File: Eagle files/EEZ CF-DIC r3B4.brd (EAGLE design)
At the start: 155 x 85 mm, 244 parts, among them IC1 MC79L05, IC2 LP2951, IC3 VIPer35L, IC4 SI8233BB-D-IS1, IC5 LM5041B, IC6 IR11688STRPBF, IC7 TL072, IC8 TL103W, IC9 TL431, P1 T910W-50K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

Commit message: Optional temperature alarm
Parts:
- added C75: 100n, rcl:C0603
- added IC10: LM211PWR, EEZ_Lib1:PW8_TSSOP8
- added NTC1: 10K, EEZ_Lib1:R_0805
- added R81: 100K, rcl:R0805
- added R82, R84: 10K, rcl:R0805
- added R83: N.C., rcl:R0805
- R15: value N.C. -> 10K
- R16: value 10K -> N.C.
- R80: value N.C. -> 1K
- moved EEZ_SIGNATURE 138.4 mm to (156.0, 76.6), turned to 270 degrees
- moved R15 58.6 mm to (13.7, 57.0), flipped to the bottom, turned to 270 degrees
- moved R16 58.6 mm to (70.3, 72.1), flipped to the top, turned to 90 degrees
- moved R80 7.85 mm to (24.3, 41.1), turned to 90 degrees
- moved R71 1.94 mm to (59.9, 29.3), turned to 0 degrees
- moved C72 1.39 mm to (56.1, 33.0), turned to 90 degrees
- moved R72 1.39 mm to (58.0, 33.0), turned to 90 degrees
- moved R65 1.06 mm to (55.9, 29.3), turned to 0 degrees
- moved C58 0.51 mm to (11.0, 42.6)
- moved R57 0.45 mm to (48.6, 8.76)
- moved Q8 0.45 mm to (42.1, 20.4)
- moved R56 0.44 mm to (44.6, 8.76)
- moved C46 0.38 mm to (87.2, 35.9)
- moved C67 0.38 mm to (47.6, 40.2)
- moved C59 0.32 mm to (10.5, 44.8)
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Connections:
- new net +2.5VREF: C72.1, IC8.3, NTC1.1, P1.E, R66.2, R72.1, R80.2
- new net N$34: IC10.3, NTC1.2, R84.2
- net AUX: now also R16.2; no longer R15.2
- net FB: now also R83.2; no longer R80.2
- net GND: now also C75.2, IC10.1, IC10.4, R82.2, R83.1, R84.1; no longer R80.1
- net N$141: now also R16.1; no longer R15.1
- net N$7: now also IC10.2, R80.1, R81.2, R82.1; no longer C72.1, IC8.3, P1.E, R66.2, R72.1
- net PWRGOOD: now also IC10.7, R15.2, R81.1; no longer R16.2
- net V+: now also C75.1, IC10.8, R15.1; no longer R16.1
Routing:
- net +2.5VREF: track 0.00 -> 86.2 mm, vias 0 -> 6
- net N$7: track 66.4 -> 11.0 mm, vias 5 -> 0
- net N$34: track 0.00 -> 32.0 mm, vias 0 -> 1
- net PWRGOOD: track 32.8 -> 59.0 mm, vias 2 -> 4
- net S2_OUT: track 26.6 -> 23.5 mm
- net FB: track 62.3 -> 59.4 mm
- net POUT+: track 30.1 -> 28.8 mm
- net SR_OUT2: track 5.68 -> 4.64 mm
- net S1_DOT_OUT: track 27.5 -> 28.3 mm
- net GND: track 132.2 -> 132.3 mm, vias 12 -> 13
- net V+: track 149.8 -> 149.9 mm, vias 3 -> 4
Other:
- board text added: "(08/2018 r3B4)"
- board text added: "C75"
- board text added: "IC10"
- board text added: "NTC1"
- board text added: "R81"
- board text added: "R82"
- board text added: "R83"
- board text added: "R84"
- board text removed: "(08/2018 r3B3)"

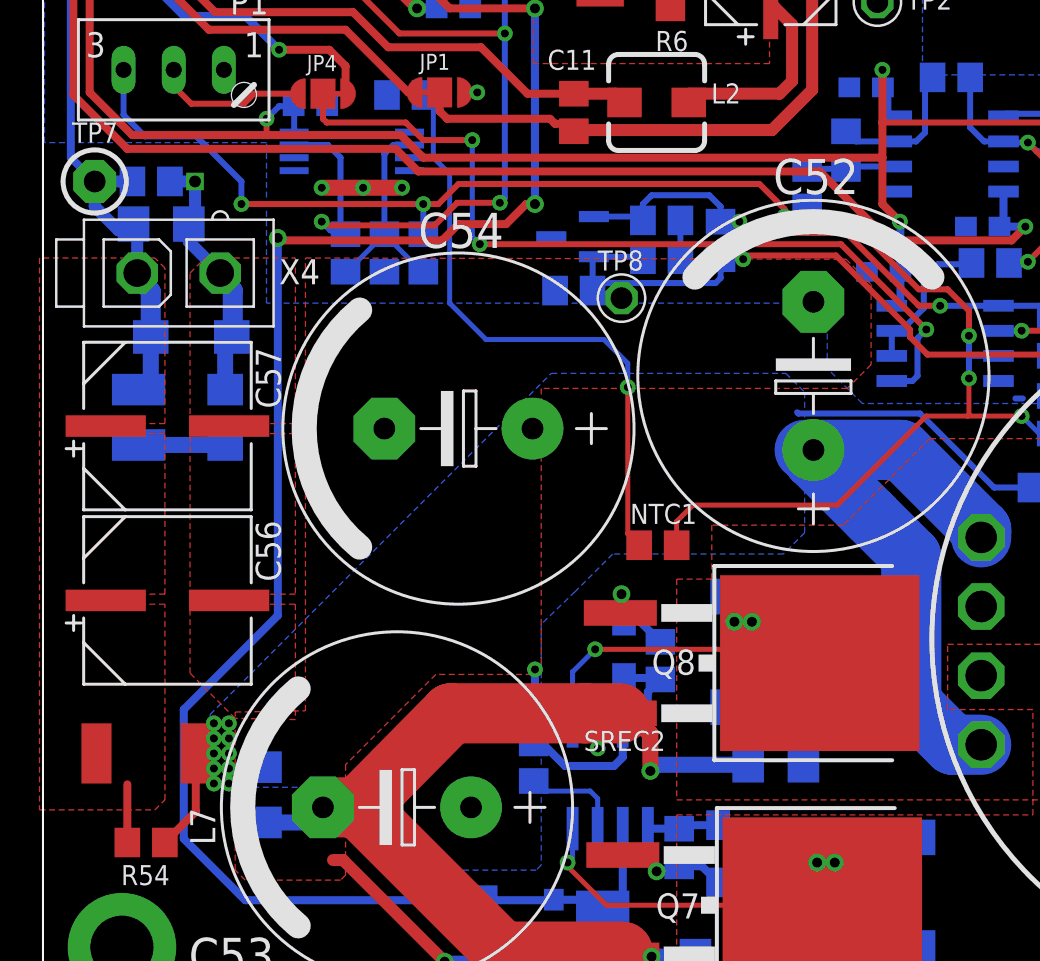
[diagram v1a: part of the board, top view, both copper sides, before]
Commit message: New values for temp. comparator
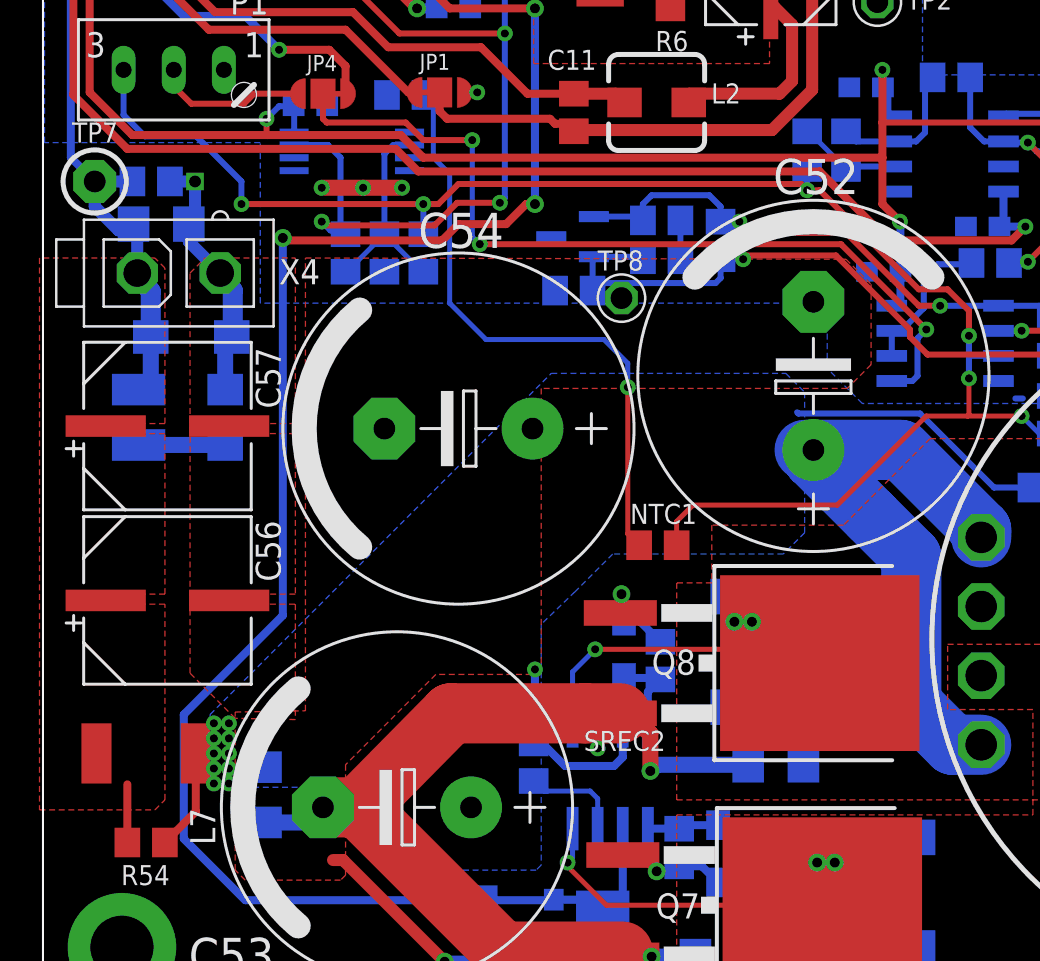
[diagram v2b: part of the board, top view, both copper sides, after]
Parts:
- NTC1: value 10K -> 10K/3570K
- R80: value 1K -> 3K9
- R81: value 100K -> 82K
- R82: value 10K -> 27K
- moved R66 1.90 mm to (43.7, 46.4)
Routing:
- net N$132: track 4.59 -> 5.38 mm
- net +2.5VREF: track 86.2 -> 85.5 mm
